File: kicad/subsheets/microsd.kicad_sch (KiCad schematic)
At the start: 17 parts

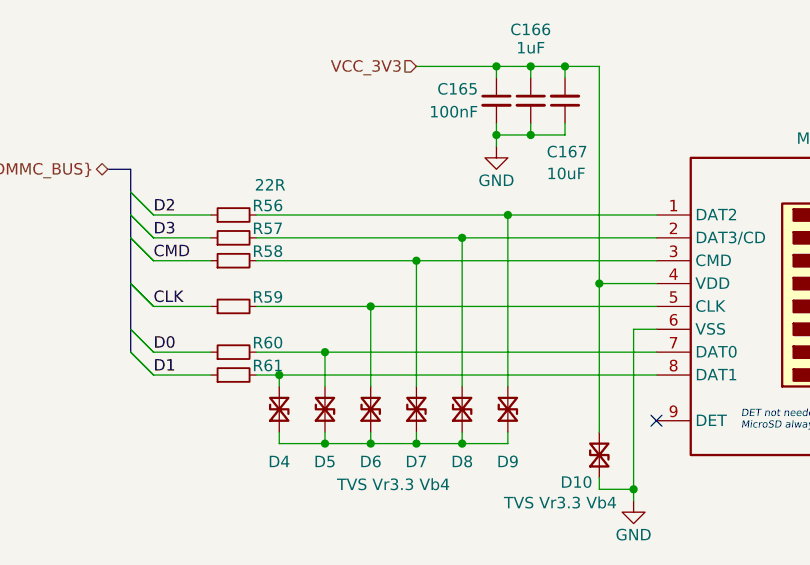
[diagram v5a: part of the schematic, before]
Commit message: Remove power/decoupling for unused power domains
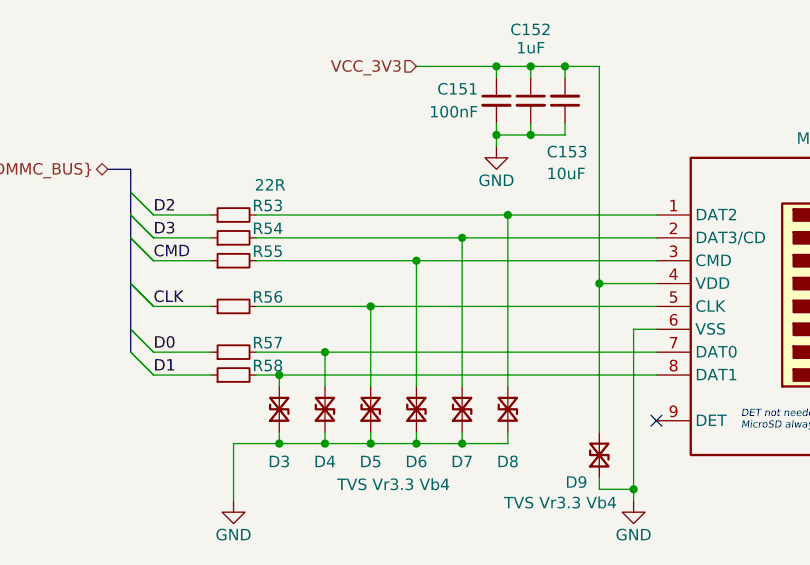
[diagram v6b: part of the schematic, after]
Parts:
- renumbered C165 to C151, C166 to C152, C167 to C153, D4 to D3, D5 to D4, D6 to D5, D7 to D6, D8 to D7, D9 to D8, D10 to D9, R56 to R53, R57 to R54, R58 to R55, R59 to R56, R60 to R57, R61 to R58
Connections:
- net GND: now also D3.1 (A1), D4.1 (A1), D5.1 (A1), D6.1 (A1), D7.1 (A1), D8.1 (A1)
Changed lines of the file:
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@@
 	)
 	(junction
+		(at 118.11 116.84)
+		(diameter 0)
+		(color 0 0 0 0)
+	)
+	(junction
 		(at 146.05 82.55)
 		(diameter 0)
@@
 	(wire
 		(pts
+			(xy 113.03 123.19) (xy 113.03 116.84)
+		)
+		(stroke
+			(width 0)
+			(type default)
+		)
+	)
+	(wire
+		(pts
 			(xy 146.05 82.55) (xy 149.86 82.55)
 		)
@@
 	(wire
 		(pts
+			(xy 113.03 116.84) (xy 118.11 116.84)
+		)
+		(stroke
+			(width 0)
+			(type default)
+		)
+	)
+	(wire
+		(pts
 			(xy 153.67 74.93) (xy 153.67 99.06)
 		)
@@
 		(on_board yes)
 		(dnp no)
-		(property "Reference" "D7"
+		(property "Reference" "D6"
 			(at 133.35 118.872 90)
 			(effects
@@
 			(project "srad-camera"
 				(path "/da62c771-e8c9-451f-8df1-ec995aadcb11/f62984d3-000f-4116-a13f-09b83b0ce025"
-					(reference "D7")
+					(reference "D6")
 					(unit 1)
 				)
@@
 		(on_board yes)
 		(dnp no)
-		(property "Reference" "D8"
+		(property "Reference" "D7"
 			(at 138.43 118.872 90)
 			(effects
@@
 			(project "srad-camera"
 				(path "/da62c771-e8c9-451f-8df1-ec995aadcb11/f62984d3-000f-4116-a13f-09b83b0ce025"
-					(reference "D8")
+					(reference "D7")
 					(unit 1)
 				)
@@
 		(on_board yes)
 		(dnp no)
-		(property "Reference" "#PWR0106"
+		(property "Reference" "#PWR0100"
 			(at 142.24 90.17 0)
 			(effects
@@
 			(project "srad-camera"
 				(path "/da62c771-e8c9-451f-8df1-ec995aadcb11/f62984d3-000f-4116-a13f-09b83b0ce025"
-					(reference "#PWR0106")
+					(reference "#PWR0100")
 					(unit 1)
 				)
@@
 		(on_board yes)
 		(dnp no)
-		(property "Reference" "D4"
+		(property "Reference" "D3"
 			(at 118.11 118.872 90)
 			(effects
@@
 			(project "srad-camera"
 				(path "/da62c771-e8c9-451f-8df1-ec995aadcb11/f62984d3-000f-4116-a13f-09b83b0ce025"
-					(reference "D4")
+					(reference "D3")
 					(unit 1)
 				)
@@
 		(on_board yes)
 		(dnp no)
-		(property "Reference" "D10"
+		(property "Reference" "D9"
 			(at 151.13 121.158 90)
 			(effects
@@
 			(project "srad-camera"
 				(path "/da62c771-e8c9-451f-8df1-ec995aadcb11/f62984d3-000f-4116-a13f-09b83b0ce025"
-					(reference "D10")
+					(reference "D9")
 					(unit 1)
 				)
@@
 		(on_board yes)
 		(dnp no)
-		(property "Reference" "R60"
+		(property "Reference" "R57"
 			(at 116.84 105.664 90)
 			(effects
@@
 			(project "srad-camera"
 				(path "/da62c771-e8c9-451f-8df1-ec995aadcb11/f62984d3-000f-4116-a13f-09b83b0ce025"
-					(reference "R60")
+					(reference "R57")
 					(unit 1)
 				)
@@
 		(on_board yes)
 		(dnp no)
-		(property "Reference" "#PWR0108"
+		(property "Reference" "#PWR0103"
 			(at 157.48 129.54 0)
 			(effects
@@
 			(project "srad-camera"
 				(path "/da62c771-e8c9-451f-8df1-ec995aadcb11/f62984d3-000f-4116-a13f-09b83b0ce025"
-					(reference "#PWR0108")
+					(reference "#PWR0103")
 					(unit 1)
 				)
@@
 		(on_board yes)
 		(dnp no)
-		(property "Reference" "R59"
+		(property "Reference" "R56"
 			(at 116.84 100.584 90)
 			(effects
@@
 			(project "srad-camera"
 				(path "/da62c771-e8c9-451f-8df1-ec995aadcb11/f62984d3-000f-4116-a13f-09b83b0ce025"
-					(reference "R59")
+					(reference "R56")
 					(unit 1)
 				)
@@
 		(on_board yes)
 		(dnp no)
-		(property "Reference" "C167"
+		(property "Reference" "C153"
 			(at 147.828 84.4437 0)
 			(effects
@@
 			(project "srad-camera"
 				(path "/da62c771-e8c9-451f-8df1-ec995aadcb11/f62984d3-000f-4116-a13f-09b83b0ce025"
-					(reference "C167")
+					(reference "C153")
 					(unit 1)
 				)
@@
 		(on_board yes)
 		(dnp no)
-		(property "Reference" "D9"
+		(property "Reference" "D8"
 			(at 143.51 118.872 90)
 			(effects
@@
 			(project "srad-camera"
 				(path "/da62c771-e8c9-451f-8df1-ec995aadcb11/f62984d3-000f-4116-a13f-09b83b0ce025"
-					(reference "D9")
+					(reference "D8")
 					(unit 1)
 				)
@@
 		(on_board yes)
 		(dnp no)
-		(property "Reference" "#PWR0107"
+		(property "Reference" "#PWR0101"
 			(at 205.74 124.46 0)
 			(effects
@@
 			(project "srad-camera"
 				(path "/da62c771-e8c9-451f-8df1-ec995aadcb11/f62984d3-000f-4116-a13f-09b83b0ce025"
-					(reference "#PWR0107")
+					(reference "#PWR0101")
 					(unit 1)
 				)
@@
 		(on_board yes)
 		(dnp no)
-		(property "Reference" "R58"
+		(property "Reference" "R55"
 			(at 116.84 95.504 90)
 			(effects
@@
 			(project "srad-camera"
 				(path "/da62c771-e8c9-451f-8df1-ec995aadcb11/f62984d3-000f-4116-a13f-09b83b0ce025"
-					(reference "R58")
+					(reference "R55")
 					(unit 1)
 				)
@@
 		(on_board yes)
 		(dnp no)
-		(property "Reference" "C165"
+		(property "Reference" "C151"
 			(at 140.208 77.47 0)
 			(effects
@@
 			(project "srad-camera"
 				(path "/da62c771-e8c9-451f-8df1-ec995aadcb11/f62984d3-000f-4116-a13f-09b83b0ce025"
-					(reference "C165")
+					(reference "C151")
 					(unit 1)
 				)
@@
 		(on_board yes)
 		(dnp no)
-		(property "Reference" "R61"
+		(property "Reference" "R58"
 			(at 116.84 108.204 90)
 			(effects
@@
 			(project "srad-camera"
 				(path "/da62c771-e8c9-451f-8df1-ec995aadcb11/f62984d3-000f-4116-a13f-09b83b0ce025"
-					(reference "R61")
+					(reference "R58")
 					(unit 1)
 				)
@@
 		(on_board yes)
 		(dnp no)
-		(property "Reference" "D5"
+		(property "Reference" "D4"
 			(at 123.19 118.872 90)
 			(effects
@@
 			(project "srad-camera"
 				(path "/da62c771-e8c9-451f-8df1-ec995aadcb11/f62984d3-000f-4116-a13f-09b83b0ce025"
-					(reference "D5")
+					(reference "D4")
 					(unit 1)
 				)
@@
 		(on_board yes)
 		(dnp no)
-		(property "Reference" "R56"
+		(property "Reference" "R53"
 			(at 116.84 90.424 90)
 			(effects
@@
 			(project "srad-camera"
 				(path "/da62c771-e8c9-451f-8df1-ec995aadcb11/f62984d3-000f-4116-a13f-09b83b0ce025"
-					(reference "R56")
+					(reference "R53")
+					(unit 1)
+				)
+			)
+		)
+	)
+	(symbol
+		(lib_id "power:GND")
+		(at 113.03 123.19 0)
+		(unit 1)
+		(exclude_from_sim no)
+		(in_bom yes)
+		(on_board yes)
+		(dnp no)
+		(property "Reference" "#PWR0102"
+			(at 113.03 129.54 0)
+			(effects
+				(font
+					(size 1.27 1.27)
+				)
+				(hide yes)
+			)
+		)
+		(property "Value" "GND"
+			(at 113.03 127 0)
+			(effects
+				(font
+					(size 1.27 1.27)
+				)
+			)
+		)
+		(property "Footprint" ""
+			(at 113.03 123.19 0)
+			(effects
+				(font
+					(size 1.27 1.27)
+				)
+				(hide yes)
+			)
+		)
+		(property "Datasheet" ""
+			(at 113.03 123.19 0)
+			(effects
+				(font
+					(size 1.27 1.27)
+				)
+				(hide yes)
+			)
+		)
+		(property "Description" ""
+			(at 113.03 123.19 0)
+			(effects
+				(font
+					(size 1.27 1.27)
+				)
+			)
+		)
+		(pin "1"
+		)
+		(instances
+			(project "srad-camera"
+				(path "/da62c771-e8c9-451f-8df1-ec995aadcb11/f62984d3-000f-4116-a13f-09b83b0ce025"
+					(reference "#PWR0102")
 					(unit 1)
 				)
@@
 		(on_board yes)
 		(dnp no)
-		(property "Reference" "D6"
+		(property "Reference" "D5"
 			(at 128.27 118.872 90)
 			(effects
@@
 			(project "srad-camera"
 				(path "/da62c771-e8c9-451f-8df1-ec995aadcb11/f62984d3-000f-4116-a13f-09b83b0ce025"
-					(reference "D6")
+					(reference "D5")
 					(unit 1)
 				)
@@
 		(on_board yes)
 		(dnp no)
-		(property "Reference" "R57"
+		(property "Reference" "R54"
 			(at 116.84 92.964 90)
 			(effects
@@
 			(project "srad-camera"
 				(path "/da62c771-e8c9-451f-8df1-ec995aadcb11/f62984d3-000f-4116-a13f-09b83b0ce025"
-					(reference "R57")
+					(reference "R54")
 					(unit 1)
 				)
@@
 		(on_board yes)
 		(dnp no)
-		(property "Reference" "C166"
+		(property "Reference" "C152"
 			(at 146.05 70.866 0)
 			(effects
@@
 			(project "srad-camera"
 				(path "/da62c771-e8c9-451f-8df1-ec995aadcb11/f62984d3-000f-4116-a13f-09b83b0ce025"
-					(reference "C166")
+					(reference "C152")
 					(unit 1)
 				)
